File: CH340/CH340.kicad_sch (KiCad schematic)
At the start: 11 parts, among them J2001 USB_B_Mini, U2001 CH340G, Y2001 Crystal

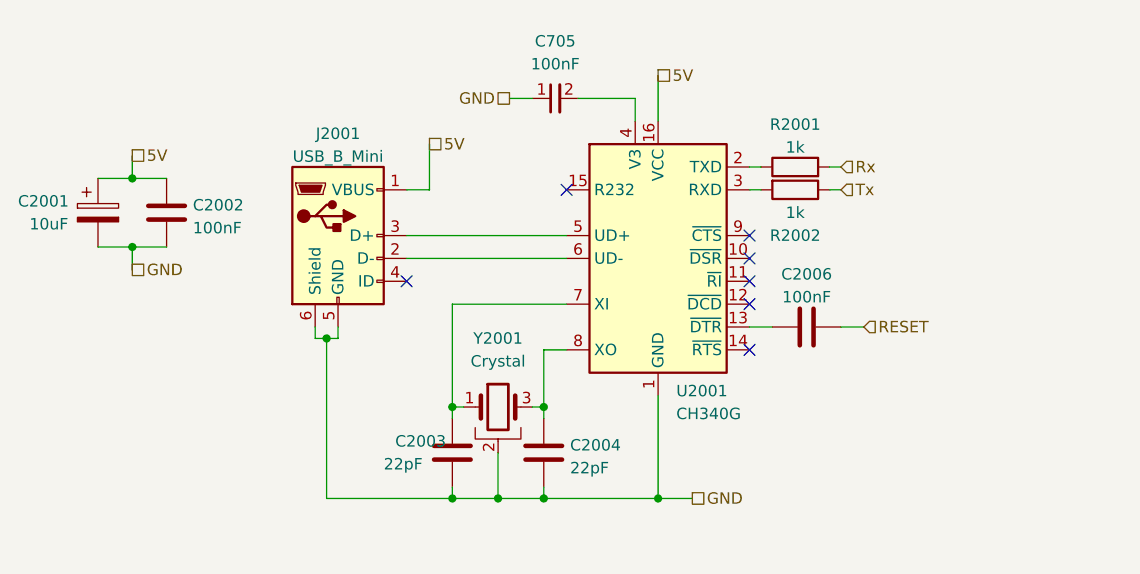
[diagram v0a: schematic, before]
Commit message: removed hierarchial labels for power symbols and replaced them with actual power symbols also updated footprint of the inductor of the 5V buck
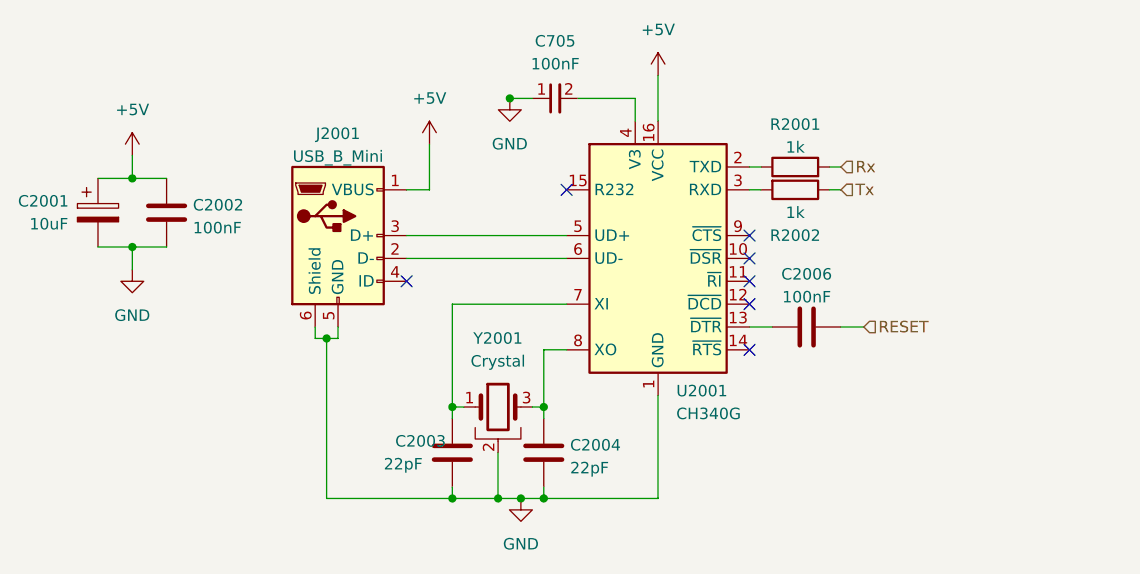
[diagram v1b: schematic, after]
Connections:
- net 5V renamed +5V
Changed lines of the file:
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@@
 (kicad_sch (version 20230121) (generator eeschema)
   (paper "A4")
+  (junction (at 106.7169 73.66) (diameter 0) (color 0 0 0 0)
+  )
   (junction (at 100.33 118.11) (diameter 0) (color 0 0 0 0)
   )
@@
   (junction (at 64.77 82.55) (diameter 0) (color 0 0 0 0)
   )
-  (junction (at 123.19 118.11) (diameter 0) (color 0 0 0 0)
+  (junction (at 107.95 118.11) (diameter 0) (color 0 0 0 0)
   )
   (junction (at 110.49 107.95) (diameter 0) (color 0 0 0 0)
@@
     (stroke (width 0) (type default))
   )
-  (wire (pts (xy 105.41 118.11) (xy 110.49 118.11))
+  (wire (pts (xy 97.79 78.74) (xy 97.79 83.82))
+    (stroke (width 0) (type default))
+  )
+  (wire (pts (xy 105.41 118.11) (xy 107.95 118.11))
     (stroke (width 0) (type default))
   )
@@
     (stroke (width 0) (type default))
   )
+  (wire (pts (xy 106.7169 73.66) (xy 109.22 73.66))
+    (stroke (width 0) (type default))
+  )
   (wire (pts (xy 134.62 83.82) (xy 133.35 83.82))
     (stroke (width 0) (type default))
   )
+  (wire (pts (xy 64.77 80.01) (xy 64.77 82.55))
+    (stroke (width 0) (type default))
+  )
   (wire (pts (xy 100.33 118.11) (xy 105.41 118.11))
     (stroke (width 0) (type default))
@@
     (stroke (width 0) (type default))
   )
+  (wire (pts (xy 107.95 118.11) (xy 110.49 118.11))
+    (stroke (width 0) (type default))
+  )
   (wire (pts (xy 143.51 83.82) (xy 142.24 83.82))
     (stroke (width 0) (type default))
@@
     (stroke (width 0) (type default))
   )
-  (wire (pts (xy 123.19 118.11) (xy 127 118.11))
-    (stroke (width 0) (type default))
-  )
   (wire (pts (xy 86.36 118.11) (xy 100.33 118.11))
     (stroke (width 0) (type default))
@@
     (stroke (width 0) (type default))
   )
-  (wire (pts (xy 64.77 80.01) (xy 64.77 82.55))
-    (stroke (width 0) (type default))
-  )
   (wire (pts (xy 95.25 88.9) (xy 113.03 88.9))
     (stroke (width 0) (type default))
   )
-  (wire (pts (xy 106.68 73.66) (xy 109.22 73.66))
+  (wire (pts (xy 106.68 73.66) (xy 106.7169 73.66))
     (stroke (width 0) (type default))
   )
@@
     (stroke (width 0) (type default))
   )
-  (wire (pts (xy 97.79 78.74) (xy 97.79 83.82))
-    (stroke (width 0) (type default))
-  )
   (wire (pts (xy 143.51 81.28) (xy 142.24 81.28))
     (stroke (width 0) (type default))
@@
   (wire (pts (xy 86.36 100.33) (xy 87.63 100.33))
     (stroke (width 0) (type default))
-  )
-  (hierarchical_label "GND" (shape passive) (at 106.68 73.66 180) (fields_autoplaced)
-    (effects (font (size 1.27 1.27)) (justify right))
-  )
-  (hierarchical_label "5V" (shape passive) (at 64.77 80.01 0) (fields_autoplaced)
-    (effects (font (size 1.27 1.27)) (justify left))
-  )
-  (hierarchical_label "5V" (shape passive) (at 123.19 71.12 0) (fields_autoplaced)
-    (effects (font (size 1.27 1.27)) (justify left))
-  )
-  (hierarchical_label "GND" (shape passive) (at 64.77 92.71 0) (fields_autoplaced)
-    (effects (font (size 1.27 1.27)) (justify left))
   )
   (hierarchical_label "Rx" (shape input) (at 143.51 81.28 0) (fields_autoplaced)
@@
     (effects (font (size 1.27 1.27)) (justify left))
   )
-  (hierarchical_label "GND" (shape passive) (at 127 118.11 0) (fields_autoplaced)
-    (effects (font (size 1.27 1.27)) (justify left))
-  )
-  (hierarchical_label "5V" (shape passive) (at 97.79 78.74 0) (fields_autoplaced)
-    (effects (font (size 1.27 1.27)) (justify left))
-  )
   (symbol (lib_id "Device:C") (at 68.58 86.36 0) (unit 1)
     (in_bom yes) (on_board yes) (dnp no) (fields_autoplaced)
@@
         (path "/fffcb7a4-8d9e-4797-952f-70897aee5417"
           (reference "C706") (unit 1)
+        )
+      )
+    )
+  )
+  (symbol (lib_name "GND_1") (lib_id "power:GND") (at 106.7169 73.66 0) (unit 1)
+    (in_bom yes) (on_board yes) (dnp no) (fields_autoplaced)
+    (property "Reference" "#PWR0207" (at 106.7169 80.01 0)
+      (effects (font (size 1.27 1.27)) hide)
+    )
+    (property "Value" "GND" (at 106.7169 78.74 0)
+      (effects (font (size 1.27 1.27)))
+    )
+    (property "Footprint" "" (at 106.7169 73.66 0)
+      (effects (font (size 1.27 1.27)) hide)
+    )
+    (property "Datasheet" "" (at 106.7169 73.66 0)
+      (effects (font (size 1.27 1.27)) hide)
+    )
+    (pin "1")
+    (instances
+      (project "atmega328"
+        (path "/8e079fd1-98e3-4beb-9638-08f2e3990e09"
+          (reference "#PWR0207") (unit 1)
+        )
+      )
+      (project "CH340"
+        (path "/fffcb7a4-8d9e-4797-952f-70897aee5417"
+          (reference "#PWR0703") (unit 1)
         )
       )
@@
     )
   )
+  (symbol (lib_name "GND_1") (lib_id "power:GND") (at 64.77 92.71 0) (unit 1)
+    (in_bom yes) (on_board yes) (dnp no) (fields_autoplaced)
+    (property "Reference" "#PWR0207" (at 64.77 99.06 0)
+      (effects (font (size 1.27 1.27)) hide)
+    )
+    (property "Value" "GND" (at 64.77 97.79 0)
+      (effects (font (size 1.27 1.27)))
+    )
+    (property "Footprint" "" (at 64.77 92.71 0)
+      (effects (font (size 1.27 1.27)) hide)
+    )
+    (property "Datasheet" "" (at 64.77 92.71 0)
+      (effects (font (size 1.27 1.27)) hide)
+    )
+    (pin "1")
+    (instances
+      (project "atmega328"
+        (path "/8e079fd1-98e3-4beb-9638-08f2e3990e09"
+          (reference "#PWR0207") (unit 1)
+        )
+      )
+      (project "CH340"
+        (path "/fffcb7a4-8d9e-4797-952f-70897aee5417"
+          (reference "#PWR0702") (unit 1)
+        )
+      )
+    )
+  )
   (symbol (lib_id "Device:C_Polarized") (at 60.96 86.36 0) (unit 1)
     (in_bom yes) (on_board yes) (dnp no)
@@
         (path "/fffcb7a4-8d9e-4797-952f-70897aee5417"
           (reference "C704") (unit 1)
+        )
+      )
+    )
+  )
+  (symbol (lib_id "power:+5V") (at 64.77 80.01 0) (unit 1)
+    (in_bom yes) (on_board yes) (dnp no) (fields_autoplaced)
+    (property "Reference" "#PWR0704" (at 64.77 83.82 0)
+      (effects (font (size 1.27 1.27)) hide)
+    )
+    (property "Value" "+5V" (at 64.77 74.93 0)
+      (effects (font (size 1.27 1.27)))
+    )
+    (property "Footprint" "" (at 64.77 80.01 0)
+      (effects (font (size 1.27 1.27)) hide)
+    )
+    (property "Datasheet" "" (at 64.77 80.01 0)
+      (effects (font (size 1.27 1.27)) hide)
+    )
+    (pin "1")
+    (instances
+      (project "CH340"
+        (path "/fffcb7a4-8d9e-4797-952f-70897aee5417"
+          (reference "#PWR0704") (unit 1)
         )
       )
@@
     )
   )
+  (symbol (lib_id "power:+5V") (at 97.79 78.74 0) (unit 1)
+    (in_bom yes) (on_board yes) (dnp no) (fields_autoplaced)
+    (property "Reference" "#PWR0706" (at 97.79 82.55 0)
+      (effects (font (size 1.27 1.27)) hide)
+    )
+    (property "Value" "+5V" (at 97.79 73.66 0)
+      (effects (font (size 1.27 1.27)))
+    )
+    (property "Footprint" "" (at 97.79 78.74 0)
+      (effects (font (size 1.27 1.27)) hide)
+    )
+    (property "Datasheet" "" (at 97.79 78.74 0)
+      (effects (font (size 1.27 1.27)) hide)
+    )
+    (pin "1")
+    (instances
+      (project "CH340"
+        (path "/fffcb7a4-8d9e-4797-952f-70897aee5417"
+          (reference "#PWR0706") (unit 1)
+        )
+      )
+    )
+  )
   (symbol (lib_id "Device:C") (at 100.33 113.03 0) (unit 1)
     (in_bom yes) (on_board yes) (dnp no)
@@
     )
   )
+  (symbol (lib_name "GND_1") (lib_id "power:GND") (at 107.95 118.11 0) (unit 1)
+    (in_bom yes) (on_board yes) (dnp no) (fields_autoplaced)
+    (property "Reference" "#PWR0207" (at 107.95 124.46 0)
+      (effects (font (size 1.27 1.27)) hide)
+    )
+    (property "Value" "GND" (at 107.95 123.19 0)
+      (effects (font (size 1.27 1.27)))
+    )
+    (property "Footprint" "" (at 107.95 118.11 0)
+      (effects (font (size 1.27 1.27)) hide)
+    )
+    (property "Datasheet" "" (at 107.95 118.11 0)
+      (effects (font (size 1.27 1.27)) hide)
+    )
+    (pin "1")
+    (instances
+      (project "atmega328"
+        (path "/8e079fd1-98e3-4beb-9638-08f2e3990e09"
+          (reference "#PWR0207") (unit 1)
+        )
+      )
+      (project "CH340"
+        (path "/fffcb7a4-8d9e-4797-952f-70897aee5417"
+          (reference "#PWR0701") (unit 1)
+        )
+      )
+    )
+  )
   (symbol (lib_id "custom_kicad_lib_sk:crystal_arduino") (at 105.41 107.95 0) (unit 1)
     (in_bom yes) (on_board yes) (dnp no) (fields_autoplaced)
@@
         )
       )
+    )
+  )
+  (symbol (lib_id "power:+5V") (at 123.19 71.12 0) (unit 1)
+    (in_bom yes) (on_board yes) (dnp no) (fields_autoplaced)
+    (property "Reference" "#PWR0705" (at 123.19 74.93 0)
+      (effects (font (size 1.27 1.27)) hide)
+    )
+    (property "Value" "+5V" (at 123.19 66.04 0)
+      (effects (font (size 1.27 1.27)))
+    )
+    (property "Footprint" "" (at 123.19 71.12 0)
+      (effects (font (size 1.27 1.27)) hide)
+    )
+    (property "Datasheet" "" (at 123.19 71.12 0)
+      (effects (font (size 1.27 1.27)) hide)
+    )
+    (pin "1")
+    (instances
+      (project "CH340"
+        (path "/fffcb7a4-8d9e-4797-952f-70897aee5417"
+          (reference "#PWR0705") (unit 1)
+        )
+      )

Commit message: made some hierarchial label changes and updated atmega328
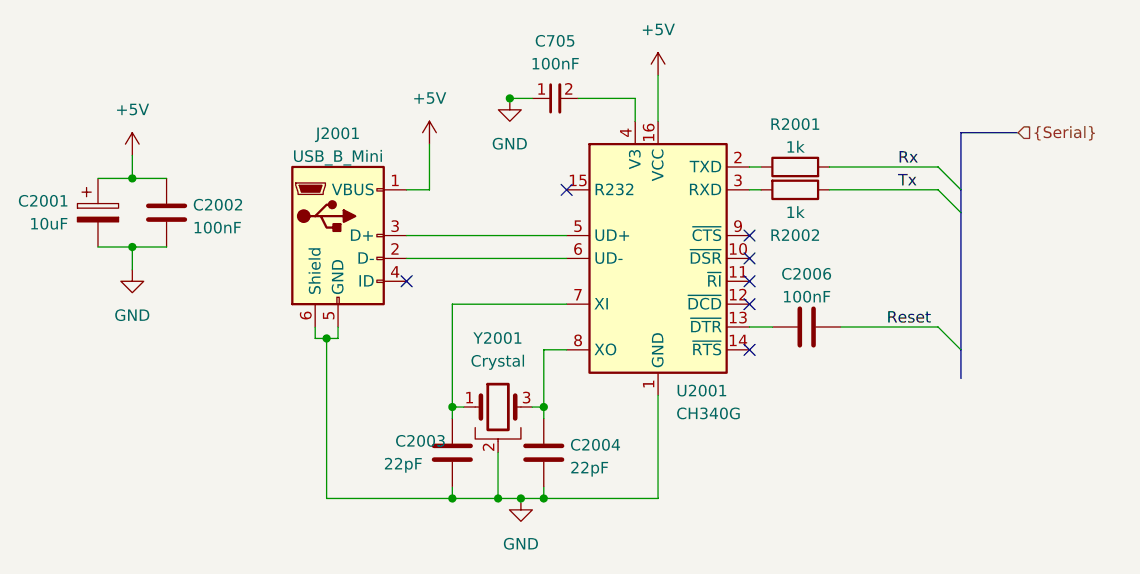
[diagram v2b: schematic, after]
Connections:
- net RESET renamed Reset
